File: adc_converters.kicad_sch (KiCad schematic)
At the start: 6 parts, among them IC1 MCP3008-I_SL, IC2 MCP3008-I_SL, IC3 MCP3008-I_SL

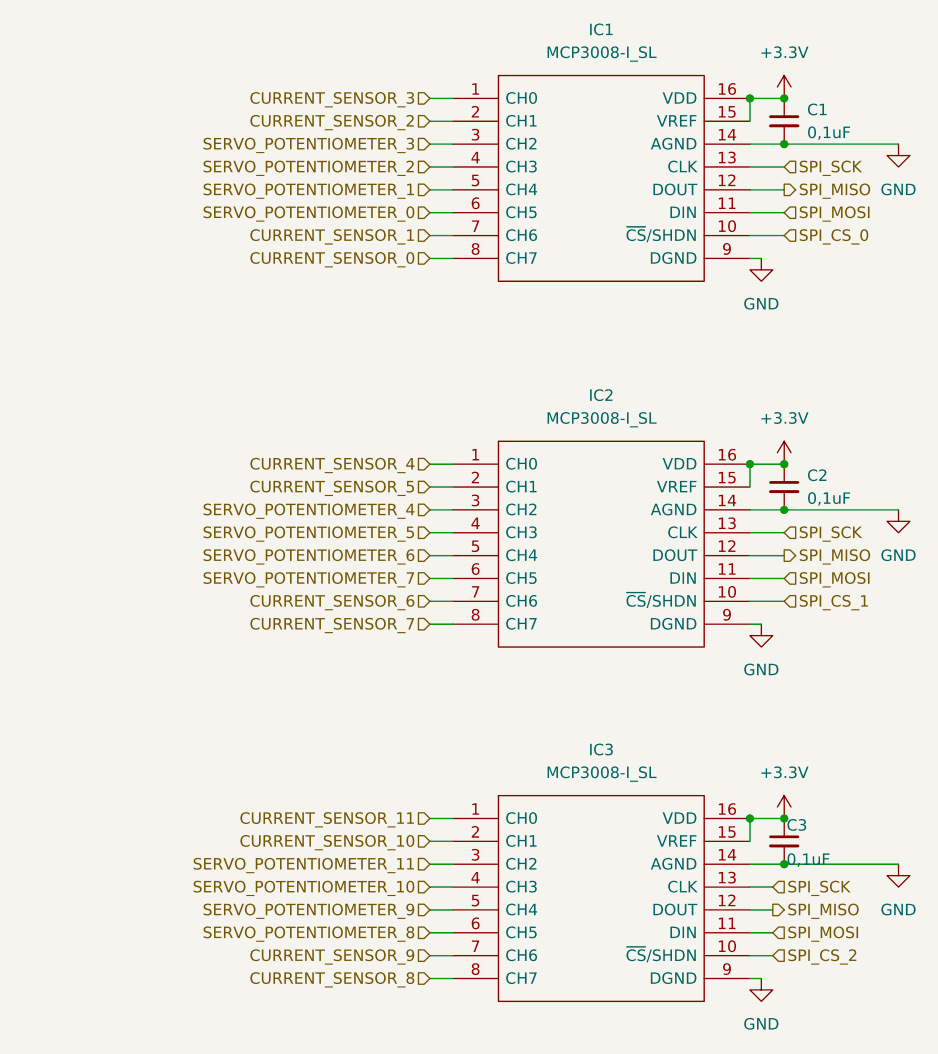
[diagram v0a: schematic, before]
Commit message: Bord v1.2, added flash memory, changed pinout od servomotor connectors and removed potentiometer signal from servomotors plus one ADC
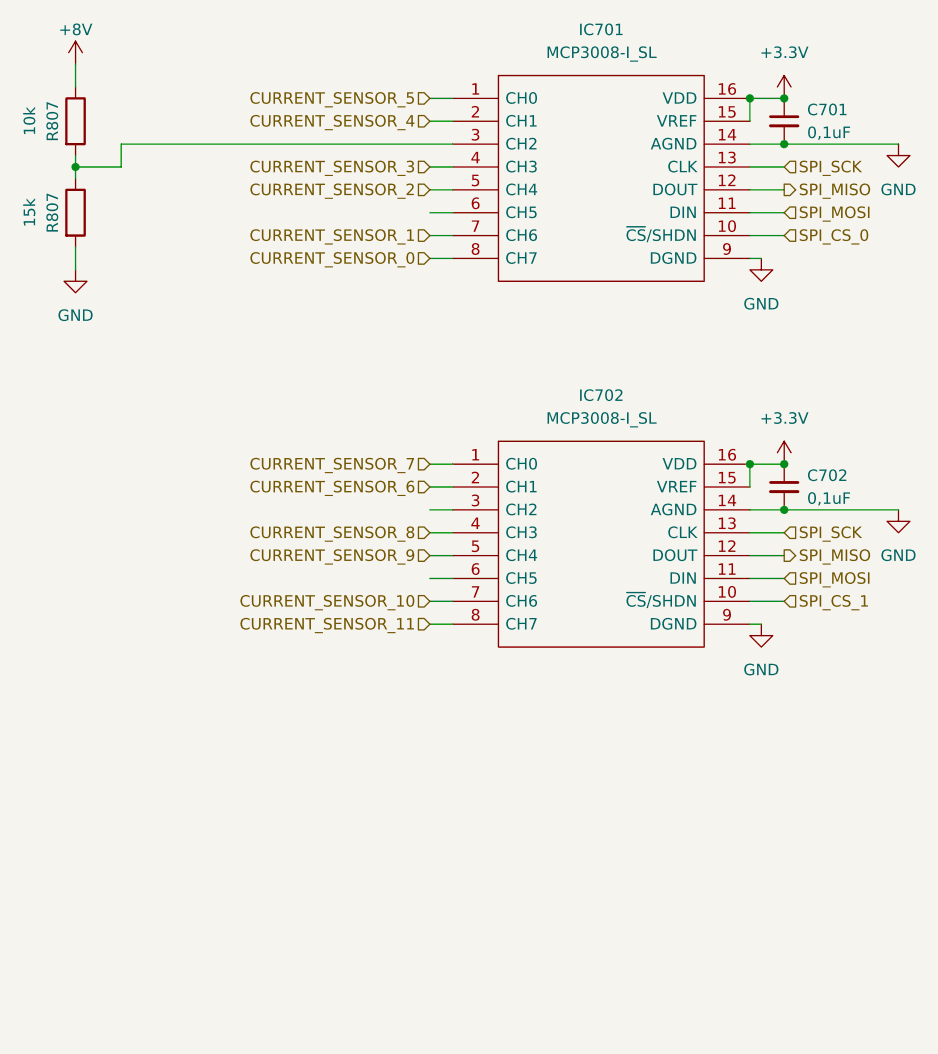
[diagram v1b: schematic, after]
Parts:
- removed C3: 0,1uF, Capacitor_SMD:C_0805_2012Metric_Pad1.18x1.45mm_HandSolder, symbol Device:C_Small
- removed IC3: MCP3008-I_SL, Package_SO:SO-16_3.9x9.9mm_P1.27mm, symbol MCP3008-I_SL:MCP3008-I_SL
- added R807: 10k, Resistor_SMD:R_1206_3216Metric_Pad1.30x1.75mm_HandSolder, symbol Device:R
- added R807: 15k, Resistor_SMD:R_1206_3216Metric_Pad1.30x1.75mm_HandSolder, symbol Device:R
- renumbered C1 to C701, C2 to C702, IC1 to IC701, IC2 to IC702
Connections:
- net SERVO_POTENTIOMETER_1 is gone; now on net CURRENT_SENSOR_2: IC701.5 (CH4)
- net SERVO_POTENTIOMETER_2 is gone; now on net CURRENT_SENSOR_3: IC701.4 (CH3)
- net SERVO_POTENTIOMETER_5 is gone; now on net CURRENT_SENSOR_8: IC702.4 (CH3)
- net SERVO_POTENTIOMETER_6 is gone; now on net CURRENT_SENSOR_9: IC702.5 (CH4)
- net CURRENT_SENSOR_10: now also IC702.7 (CH6)
- net CURRENT_SENSOR_11: now also IC702.8 (CH7)
- net CURRENT_SENSOR_2: no longer IC701.2 (CH1)
- net CURRENT_SENSOR_3: no longer IC701.1 (CH0)
- net CURRENT_SENSOR_4: now also IC701.2 (CH1); no longer IC702.1 (CH0)
- net CURRENT_SENSOR_5: now also IC701.1 (CH0); no longer IC702.2 (CH1)
- net CURRENT_SENSOR_6: now also IC702.2 (CH1); no longer IC702.7 (CH6)
- net CURRENT_SENSOR_7: now also IC702.1 (CH0); no longer IC702.8 (CH7)
- net GND: now also R807.2
- net SERVO_POTENTIOMETER_0: no longer names the net of IC701.6 (CH5)
- net SERVO_POTENTIOMETER_3: no longer names the net of IC701.3 (CH2)
- net SERVO_POTENTIOMETER_3: now also R807.1, R807.2
- net SERVO_POTENTIOMETER_4: no longer names the net of IC702.3 (CH2)
- net SERVO_POTENTIOMETER_7: no longer names the net of IC702.6 (CH5)
- new net +8V: R807.1
